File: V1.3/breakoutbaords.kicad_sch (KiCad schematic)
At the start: 10 parts, among them J13 USB_A, J3 Conn_02x19_Top_Bottom, J4 Conn_02x19_Top_Bottom, U3 AMS1117-3.3

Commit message: update v1.3 schematic documentation
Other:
- note added: "Breakout Board Connections"
- note added: "It takes more than just one board to make these controllers work."
- moved on the sheet: I2C-2, I2C-3, J13, J3, J4, R7, R8, SPI-1, U3, pwr5v1

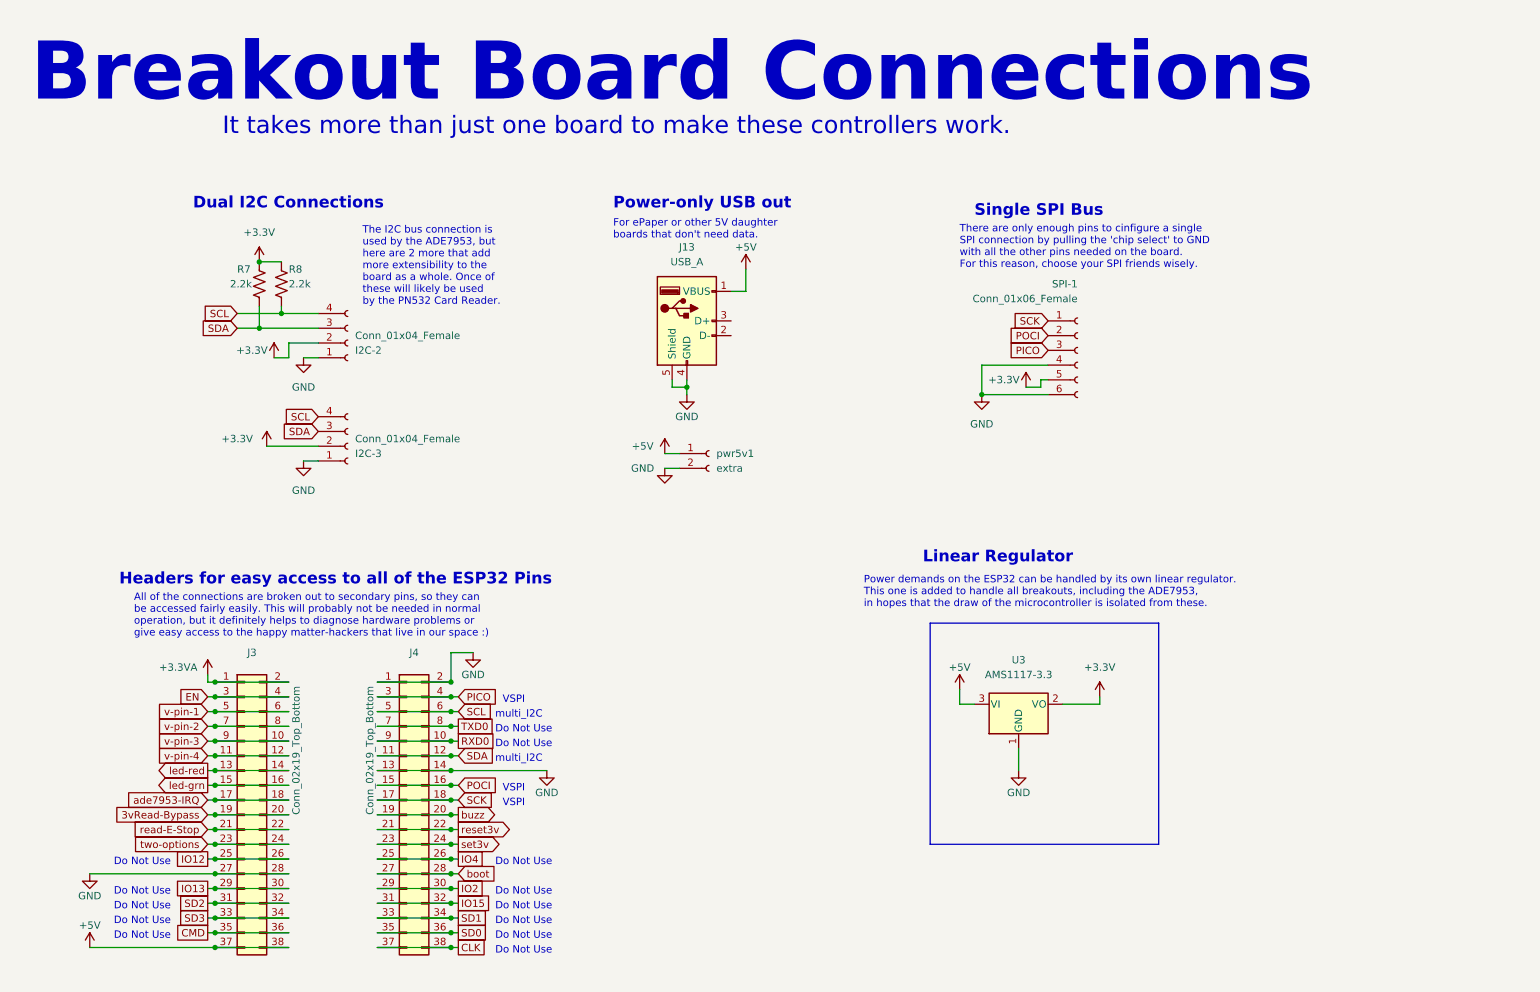
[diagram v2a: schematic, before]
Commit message: started adding the feather footprint to the board. need to update board shape and silkscreens
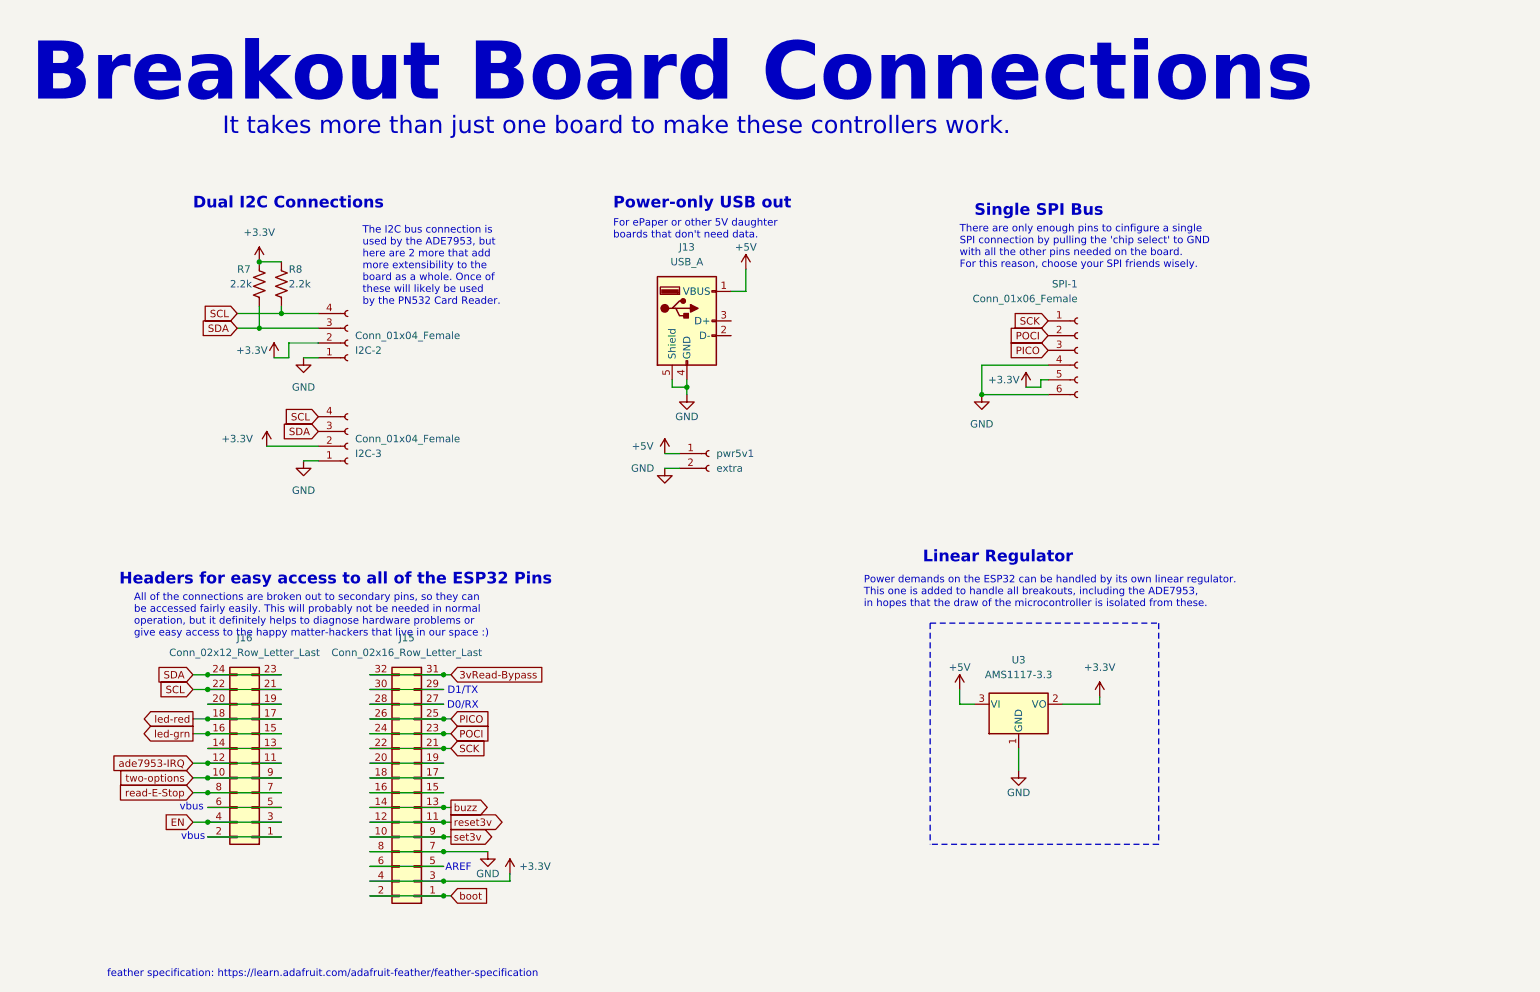
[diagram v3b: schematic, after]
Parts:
- removed J3, J4: Conn_02x19_Top_Bottom, Connector_PinSocket_2.54mm:PinSocket_2x19_P2.54mm_Vertical, symbol Connector_Generic:Conn_02x19_Odd_Even
- added J15: Conn_02x16_Row_Letter_Last, Connector_PinHeader_2.54mm:PinHeader_2x16_P2.54mm_Vertical, symbol Connector_Generic:Conn_02x16_Odd_Even
- added J16: Conn_02x12_Row_Letter_Last, Connector_PinHeader_2.54mm:PinHeader_2x12_P2.54mm_Vertical, symbol Connector_Generic:Conn_02x12_Odd_Even
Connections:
- net +3.3V: now also J15.3 (Pin_3), J15.4 (Pin_4)
- net 3vRead-Bypass: now also J15.31 (Pin_31), J15.32 (Pin_32)
- net EN: now also J16.3 (Pin_3), J16.4 (Pin_4)
- net GND: now also J15.7 (Pin_7), J15.8 (Pin_8)
- net PICO: now also J15.25 (Pin_25), J15.26 (Pin_26)
- net POCI: now also J15.23 (Pin_23), J15.24 (Pin_24)
- net SCK: now also J15.21 (Pin_21), J15.22 (Pin_22)
- net SCL: now also J16.21 (Pin_21), J16.22 (Pin_22)
- net SDA: now also J16.23 (Pin_23), J16.24 (Pin_24)
- net ade7953-IRQ: now also J16.11 (Pin_11), J16.12 (Pin_12)
- net boot: now also J15.1 (Pin_1), J15.2 (Pin_2)
- net buzz: now also J15.13 (Pin_13), J15.14 (Pin_14)
- net led-grn: now also J16.15 (Pin_15), J16.16 (Pin_16)
- net led-red: now also J16.17 (Pin_17), J16.18 (Pin_18)
- net read-E-Stop: now also J16.7 (Pin_7), J16.8 (Pin_8)
- net reset3v: now also J15.11 (Pin_11), J15.12 (Pin_12)
- net set3v: now also J15.10 (Pin_10), J15.9 (Pin_9)
- net two-options: now also J16.10 (Pin_10), J16.9 (Pin_9)
- new net: J15.15 (Pin_15), J15.16 (Pin_16)
- new net: J15.17 (Pin_17), J15.18 (Pin_18)
- new net: J15.19 (Pin_19), J15.20 (Pin_20)
- new net: J15.27 (Pin_27), J15.28 (Pin_28)
- new net: J15.29 (Pin_29), J15.30 (Pin_30)
- new net: J15.5 (Pin_5), J15.6 (Pin_6)
- new net: J16.1 (Pin_1), J16.2 (Pin_2)
- new net: J16.13 (Pin_13), J16.14 (Pin_14)
- new net: J16.19 (Pin_19), J16.20 (Pin_20)
- new net: J16.5 (Pin_5), J16.6 (Pin_6)
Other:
- note added: "AREF"
- note added: "D0/RX"
- note added: "D1/TX"
- note added: "feather specification: https://learn.adafruit.com/adafruit-feather/feather-specification"
- note added: "vbus"
- note removed: "Do Not Use"
- note removed: "VSPI"
- note removed: "multi_I2C"

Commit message: design for feather-based board should work, but nothing is pretty
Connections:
- net +3.3V: no longer J15.3 (Pin_3), J15.4 (Pin_4)
- net 3vRead-Bypass: now also J15.19 (Pin_19), J15.20 (Pin_20); no longer J15.31 (Pin_31), J15.32 (Pin_32)
- new net: J15.31 (Pin_31), J15.32 (Pin_32)
- new net +3.3VA: J15.3 (Pin_3), J15.4 (Pin_4)
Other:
- note added: "NOTE: all pins labeled with blue text should not be used in this design, as they have specified roles in feathers."
- note added: "SPARE"
- note added: "out only"
- note added: "vBATTERY"
- note added: "vUSB"
- note removed: "vbus"
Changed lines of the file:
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@@
 	)
 	(junction
-		(at 100.33 138.43)
+		(at 100.33 153.67)
 		(diameter 0)
 		(color 0 0 0 0)
@@
 	(wire
 		(pts
-			(xy 100.33 138.43) (xy 101.6 138.43)
+			(xy 100.33 153.67) (xy 101.6 153.67)
 		)
 		(stroke
@@
 	(text "D0/RX"
 		(exclude_from_sim no)
-		(at 103.632 143.764 0)
+		(at 103.886 143.764 0)
 		(effects
 			(font
@@
 			)
 			(href "https://learn.adafruit.com/adafruit-feather/feather-specification")
+		)
+	)
+	(text "out only"
+		(exclude_from_sim no)
+		(at 116.332 173.482 0)
+		(effects
+			(font
+				(size 1.27 1.27)
+			)
+			(href "https://learn.adafruit.com/adafruit-feather/feather-specification#3-dot-3v-output-2861843")
 		)
 	)
@@
 		)
 	)
-	(text " vbus"
-		(exclude_from_sim no)
-		(at 56.642 161.29 0)
+	(text " vUSB"
+		(exclude_from_sim no)
+		(at 45.466 164.084 0)
 		(effects
 			(font
@@
 		)
 	)
-	(text " vbus"
-		(exclude_from_sim no)
-		(at 56.896 166.37 0)
+	(text " vBATTERY"
+		(exclude_from_sim no)
+		(at 54.864 166.624 0)
 		(effects
 			(font
@@
 		)
 	)
+	(text "NOTE: all pins labeled with blue text\nshould not be used in this design, as \nthey have specified roles in feathers."
+		(exclude_from_sim no)
+		(at 64.008 173.736 0)
+		(effects
+			(font
+				(size 1.27 1.27)
+			)
+		)
+	)
+	(text "SPARE"
+		(exclude_from_sim no)
+		(at 103.632 138.684 0)
+		(effects
+			(font
+				(size 1.27 1.27)
+			)
+			(href "https://learn.adafruit.com/adafruit-feather/feather-specification#other-pins-2861847")
+		)
+	)
 	(global_label "SCL"
 		(shape input)
@@
 	(global_label "3vRead-Bypass"
 		(shape input)
-		(at 101.6 138.43 0)
+		(at 101.6 153.67 0)
 		(fields_autoplaced yes)
 		(effects
@@
 		)
 		(property "Intersheetrefs" "${INTERSHEET_REFS}"
-			(at 119.5831 138.43 0)
+			(at 119.5831 153.67 0)
 			(effects
 				(font
@@
 			)
 		)
-		(property "Value" "+3.3V"
+		(property "Value" "+3.3VA"
 			(at 116.078 171.45 0)
 			(effects
@@
 		)
 		(property "Value" "+3.3V"
-			(at 68.58 62.23 0)
-			(effects
-				(font
-					(size 1.27 1.27)
-				)
-			)
-		)
+			(at 71.12 66.0399 0)
+			(effects
+				(font
+					(size 1.27 1.27)
+				)
+				(justify left)
+			)
+		)

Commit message: updated USB to correct JLCPCB part #
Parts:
- J13: JLCPCB Part # C265461 -> C32896
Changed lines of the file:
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@@
 			)
 		)
-		(property "Datasheet" "https://datasheet.lcsc.com/lcsc/1811101526_JST-Sales-America-UBAS-4R-D14D-4D-LF-SN_C265461.pdf"
+		(property "Datasheet" "https://jlcpcb.com/partdetail/boomele_boom_Precision_elec-C32896/C32896"
 			(at 146.05 78.74 0)
 			(effects
@@
 			)
 		)
-		(property "JLCPCB Part #" "C265461"
+		(property "JLCPCB Part #" "C32896"
 			(at 142.24 77.47 0)
 			(effects
